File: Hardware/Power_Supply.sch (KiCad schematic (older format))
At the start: 14 parts, among them SW1 1101M2S3AQE2, U1 TPS565208DDC

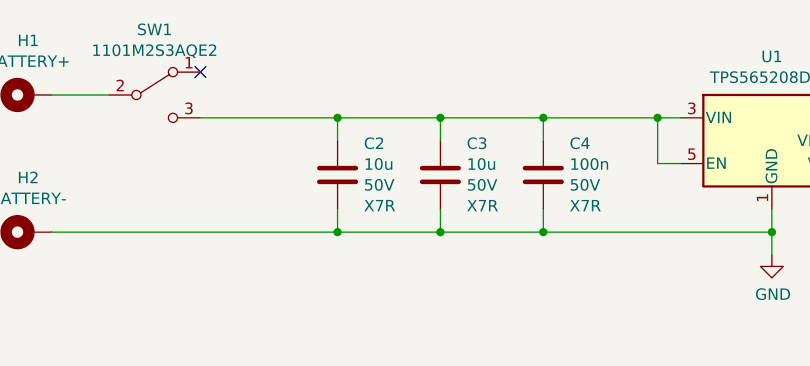
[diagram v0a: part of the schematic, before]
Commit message: [Hardware] Started ADC schematic sheet. Added ADC, voltage regulator and battery voltage sensing.
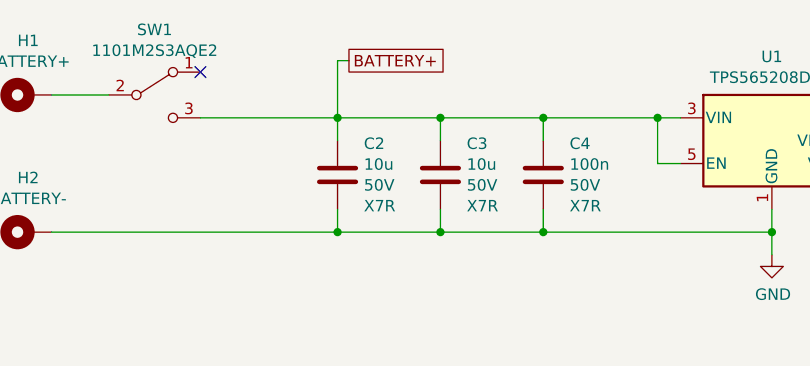
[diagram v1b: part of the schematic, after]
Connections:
- net BATTERY+: now reaches C2.2, C3.2, C4.2, SW1.3 (C), U1.3 (VIN), U1.5 (EN)
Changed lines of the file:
@@
 $Descr A4 11693 8268
 encoding utf-8
-Sheet 2 3
+Sheet 2 4
 Title "DC/DC power supply"
 Date "2020-07-27"
@@
 	2350 3350 2600 3350
 NoConn ~ 3000 3250
+Text GLabel 3650 3200 2    50   UnSpc ~ 0
+BATTERY+
+Wire Wire Line
+	3650 3200 3600 3200
+Wire Wire Line
+	3600 3200 3600 3450
 $EndSCHEMATC

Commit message: [Hardware] Added IHLP3232DZER3R3M01 inductor footprint.
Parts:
- L1: footprint (none) -> IHLP3232DZER3R3M01:IHLP3232DZER3R3M01
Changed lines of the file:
@@
 F 0 "L1" V 7290 3450 50  0000 C CNN
 F 1 "IHLP3232DZER3R3M01" V 7199 3450 50  0000 C CNN
-F 2 "" H 7100 3450 50  0001 C CNN
+F 2 "IHLP3232DZER3R3M01:IHLP3232DZER3R3M01" H 7100 3450 50  0001 C CNN
 F 3 "~" H 7100 3450 50  0001 C CNN
 F 4 "Vishay-Dale" H 7100 3450 50  0001 C CNN "Manufacturer"

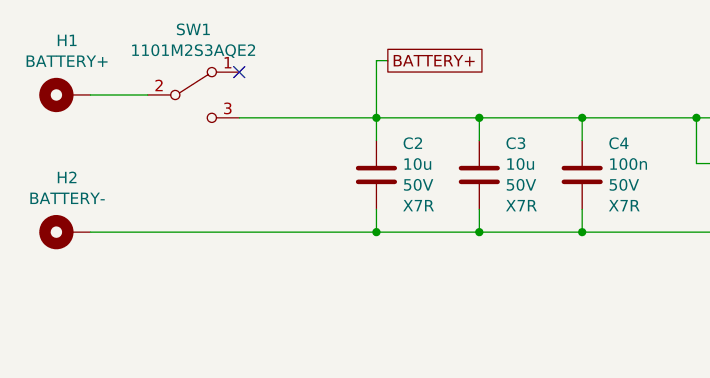
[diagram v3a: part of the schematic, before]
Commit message: [Hardware] Changed power switch pins order to ease routing.
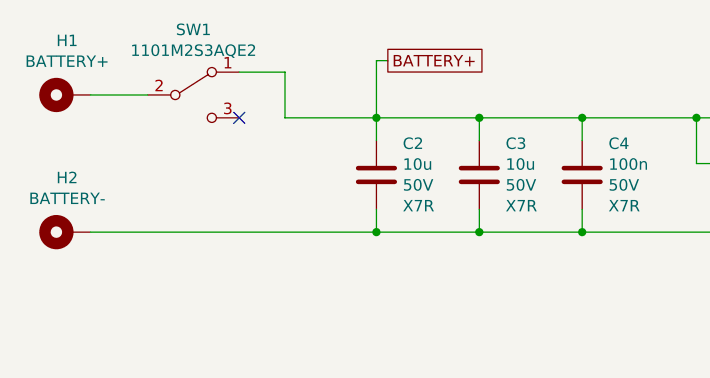
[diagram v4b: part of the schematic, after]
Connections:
- net BATTERY+: now also SW1.1 (A); no longer SW1.3 (C)
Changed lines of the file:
@@
 $EndComp
-Wire Wire Line
-	3000 3450 3600 3450
 Wire Wire Line
 	3600 3450 3600 3550
@@
 Wire Wire Line
 	2350 3350 2600 3350
-NoConn ~ 3000 3250
 Text GLabel 3650 3200 2    50   UnSpc ~ 0
 BATTERY+
@@
 Wire Wire Line
 	3600 3200 3600 3450
+Wire Wire Line
+	3000 3250 3200 3250
+Wire Wire Line
+	3200 3250 3200 3450
+Wire Wire Line
+	3200 3450 3600 3450
+NoConn ~ 3000 3450
 $EndSCHEMATC

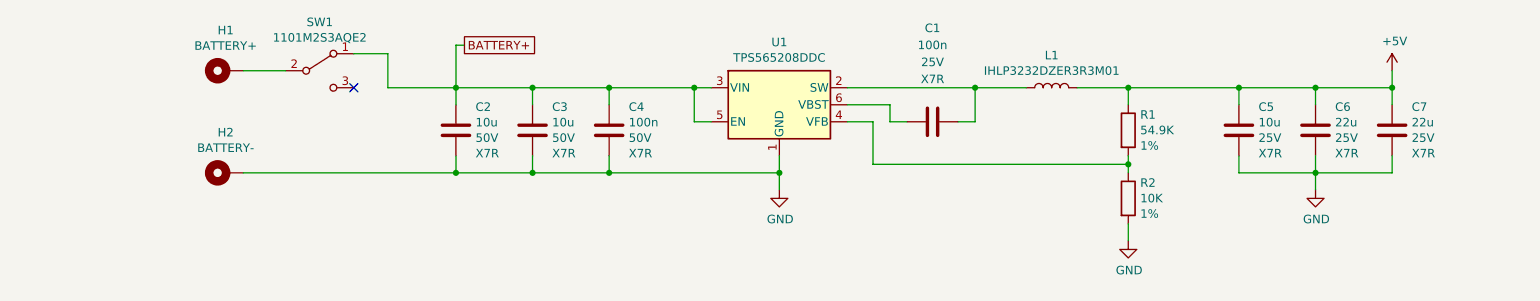
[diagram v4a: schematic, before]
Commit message: [Hardware] Removed mechanical supply parts unrelated with PCB, added battery holder supply part.
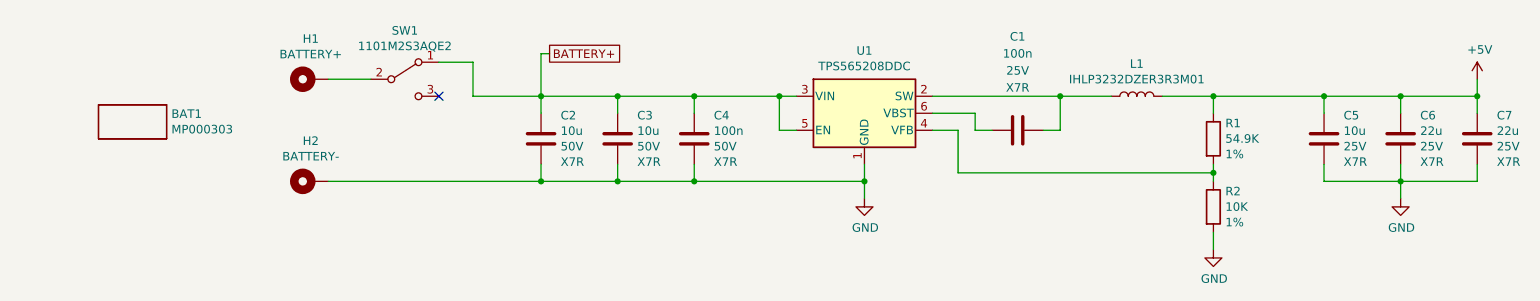
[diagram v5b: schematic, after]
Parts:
- added BAT1: MP000303, Supply_Part:Supply_Part, symbol Supply_Part:Supply_Part
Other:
- moved on the sheet: C1, C2, C3, C4, C5, C6, C7, H1, H2, L1, R1, R2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

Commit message: [Hardware] Changed 22u capacitors footprint from 1206 to 1210 as more references are available in 1210 package.
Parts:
- BAT1: Manufacturer Feetech -> MULTICOMP_PRO; Value2 Wheel -> Battery_Holder
- C6, C7: footprint Capacitor_SMD:C_1206_3216Metric_Pad1.42x1.75mm_HandSolder -> Capacitor_SMD:C_1210_3225Metric_Pad1.42x2.65mm_HandSolder
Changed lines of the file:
@@
 F 0 "C6" H 9035 3613 50  0000 R CNN
 F 1 "22u" H 9035 3704 50  0000 R CNN
-F 2 "Capacitor_SMD:C_1206_3216Metric_Pad1.42x1.75mm_HandSolder" H 9188 3600 50  0001 C CNN
+F 2 "Capacitor_SMD:C_1210_3225Metric_Pad1.42x2.65mm_HandSolder" H 9188 3600 50  0001 C CNN
 F 3 "~" H 9150 3750 50  0001 C CNN
 F 4 "25V" H 9035 3795 50  0000 R CNN "Value2"
@@
 F 0 "C7" H 9485 3613 50  0000 R CNN
 F 1 "22u" H 9485 3704 50  0000 R CNN
-F 2 "Capacitor_SMD:C_1206_3216Metric_Pad1.42x1.75mm_HandSolder" H 9638 3600 50  0001 C CNN
+F 2 "Capacitor_SMD:C_1210_3225Metric_Pad1.42x2.65mm_HandSolder" H 9638 3600 50  0001 C CNN
 F 3 "~" H 9600 3750 50  0001 C CNN
 F 4 "25V" H 9485 3795 50  0000 R CNN "Value2"
@@
 F 2 "Supply_Part:Supply_Part" H 1700 3650 50  0001 C CNN
 F 3 "" H 1700 3650 50  0001 C CNN
-F 4 "Feetech" H 1700 3650 50  0001 C CNN "Manufacturer"
-F 5 "Wheel" H 1700 3650 50  0001 C CNN "Value2"
+F 4 "MULTICOMP_PRO" H 1700 3650 50  0001 C CNN "Manufacturer"
+F 5 "Battery_Holder" H 1700 3650 50  0001 C CNN "Value2"
 	1    1700 3650
 	1    0    0    -1

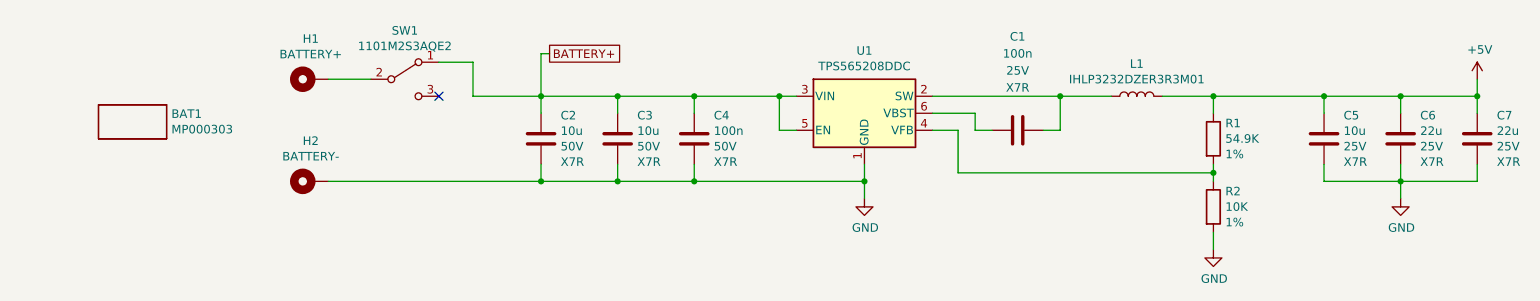
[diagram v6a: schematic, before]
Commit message: [Hardware] Added a big capacitor right after power supply switch to keep battery voltage stable during high current demands.
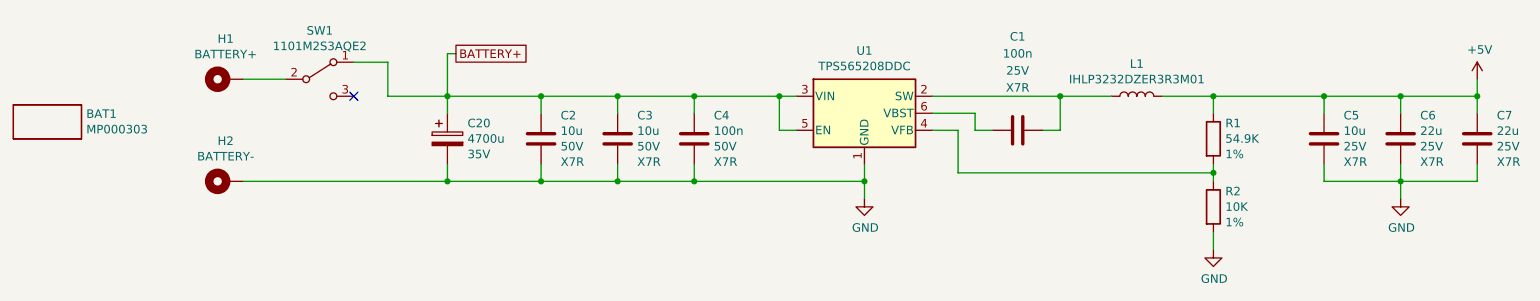
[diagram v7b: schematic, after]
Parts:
- added C20: 4700u, Capacitor_THT:CP_Radial_D16.0mm_P7.50mm, symbol Device:CP
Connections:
- net BATTERY+: now also C20.1
- net GND: now also C20.2
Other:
- moved on the sheet: BAT1, H1, H2, SW1
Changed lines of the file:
@@
 L Mechanical:MountingHole_Pad H2
 U 1 1 5F1FE00E
-P 2750 4000
-F 0 "H2" V 2987 4003 50  0000 C CNN
-F 1 "BATTERY-" V 2896 4003 50  0000 C CNN
-F 2 "MountingHole:MountingHole_2.2mm_M2_Pad" H 2750 4000 50  0001 C CNN
-F 3 "~" H 2750 4000 50  0001 C CNN
-	1    2750 4000
+P 2250 4000
+F 0 "H2" V 2487 4003 50  0000 C CNN
+F 1 "BATTERY-" V 2396 4003 50  0000 C CNN
+F 2 "MountingHole:MountingHole_2.2mm_M2_Pad" H 2250 4000 50  0001 C CNN
+F 3 "~" H 2250 4000 50  0001 C CNN
+	1    2250 4000
 	0    -1   -1   0
 $EndComp
@@
 L Mechanical:MountingHole_Pad H1
 U 1 1 5F1FF3A5
-P 2750 3400
-F 0 "H1" V 2987 3403 50  0000 C CNN
-F 1 "BATTERY+" V 2896 3403 50  0000 C CNN
-F 2 "MountingHole:MountingHole_2.2mm_M2_Pad" H 2750 3400 50  0001 C CNN
-F 3 "~" H 2750 3400 50  0001 C CNN
-	1    2750 3400
+P 2250 3400
+F 0 "H1" V 2487 3403 50  0000 C CNN
+F 1 "BATTERY+" V 2396 3403 50  0000 C CNN
+F 2 "MountingHole:MountingHole_2.2mm_M2_Pad" H 2250 3400 50  0001 C CNN
+F 3 "~" H 2250 3400 50  0001 C CNN
+	1    2250 3400
 	0    -1   -1   0
 $EndComp
@@
 Connection ~ 5000 4000
 Wire Wire Line
-	2850 4000 4100 4000
-Connection ~ 4100 4000
+	2350 4000 3550 4000
 Wire Wire Line
 	4100 4000 4550 4000
@@
 L Switch:SW_SPDT SW1
 U 1 1 5F22069E
-P 3300 3400
-F 0 "SW1" H 3300 3685 50  0000 C CNN
-F 1 "1101M2S3AQE2" H 3300 3594 50  0000 C CNN
-F 2 "1101M2S3AQE2:1101M2S3AQE2" H 3300 3400 50  0001 C CNN
-F 3 "~" H 3300 3400 50  0001 C CNN
-	1    3300 3400
-	1    0    0    -1
-$EndComp
-Wire Wire Line
-	2850 3400 3100 3400
-Text GLabel 4150 3250 2    50   UnSpc ~ 0
+P 2800 3400
+F 0 "SW1" H 2800 3685 50  0000 C CNN
+F 1 "1101M2S3AQE2" H 2800 3594 50  0000 C CNN
+F 2 "1101M2S3AQE2:1101M2S3AQE2" H 2800 3400 50  0001 C CNN
+F 3 "~" H 2800 3400 50  0001 C CNN
+	1    2800 3400
+	1    0    0    -1
+$EndComp
+Wire Wire Line
+	2350 3400 2600 3400
+Text GLabel 3600 3250 2    50   UnSpc ~ 0
 BATTERY+
 Wire Wire Line
-	4150 3250 4100 3250
-Wire Wire Line
-	4100 3250 4100 3500
-Wire Wire Line
-	3500 3300 3700 3300
-Wire Wire Line
-	3700 3300 3700 3500
-Wire Wire Line
-	3700 3500 4100 3500
-NoConn ~ 3500 3500
+	3600 3250 3550 3250
+Wire Wire Line
+	3550 3250 3550 3500
+Wire Wire Line
+	3000 3300 3200 3300
+Wire Wire Line
+	3200 3300 3200 3500
+NoConn ~ 3000 3500
 $Comp
 L Supply_Part:Supply_Part BAT?
 U 1 1 5F37F87A
-P 1700 3650
+P 1200 3650
 AR Path="/5F22814A/5F37F87A" Ref="BAT?"  Part="1"
 AR Path="/5F37F87A" Ref="BAT?"  Part="1"
 AR Path="/5F1F2F9E/5F37F87A" Ref="BAT1"  Part="1"
-F 0 "BAT1" H 1928 3696 50  0000 L CNN
-F 1 "MP000303" H 1928 3605 50  0000 L CNN
-F 2 "Supply_Part:Supply_Part" H 1700 3650 50  0001 C CNN
-F 3 "" H 1700 3650 50  0001 C CNN
-F 4 "MULTICOMP_PRO" H 1700 3650 50  0001 C CNN "Manufacturer"
-F 5 "Battery_Holder" H 1700 3650 50  0001 C CNN "Value2"
-	1    1700 3650
-	1    0    0    -1
-$EndComp
+F 0 "BAT1" H 1428 3696 50  0000 L CNN
+F 1 "MP000303" H 1428 3605 50  0000 L CNN
+F 2 "Supply_Part:Supply_Part" H 1200 3650 50  0001 C CNN
+F 3 "" H 1200 3650 50  0001 C CNN
+F 4 "MULTICOMP_PRO" H 1200 3650 50  0001 C CNN "Manufacturer"
+F 5 "Battery_Holder" H 1200 3650 50  0001 C CNN "Value2"
+	1    1200 3650
+	1    0    0    -1
+$EndComp
+$Comp
+L Device:CP C20
+U 1 1 5F467D3F
+P 3550 3750
+F 0 "C20" H 3668 3841 50  0000 L CNN
+F 1 "4700u" H 3668 3750 50  0000 L CNN
+F 2 "Capacitor_THT:CP_Radial_D16.0mm_P7.50mm" H 3588 3600 50  0001 C CNN
+F 3 "~" H 3550 3750 50  0001 C CNN
+F 4 "35V" H 3668 3659 50  0000 L CNN "Value2"
+F 5 "MCKSK035M472J32S" H 3550 3750 50  0001 C CNN "Value3"
+	1    3550 3750
+	1    0    0    -1
+$EndComp
+Wire Wire Line
+	3200 3500 3550 3500
+Wire Wire Line
+	3550 3500 4100 3500
+Connection ~ 3550 3500
+Wire Wire Line
+	3550 3500 3550 3600
+Wire Wire Line
+	3550 3900 3550 4000
+Connection ~ 3550 4000
+Connection ~ 4100 4000
+Wire Wire Line
+	3550 4000 4100 4000
 $EndSCHEMATC

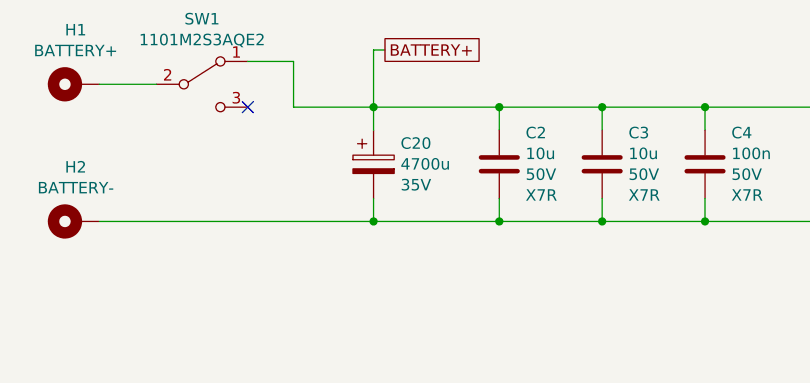
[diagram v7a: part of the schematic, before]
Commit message: [Hardware] Added big capacitor 'custom' footprint to PCB. Capacitor must be bent over SMD parts and glued like shown in pictures.
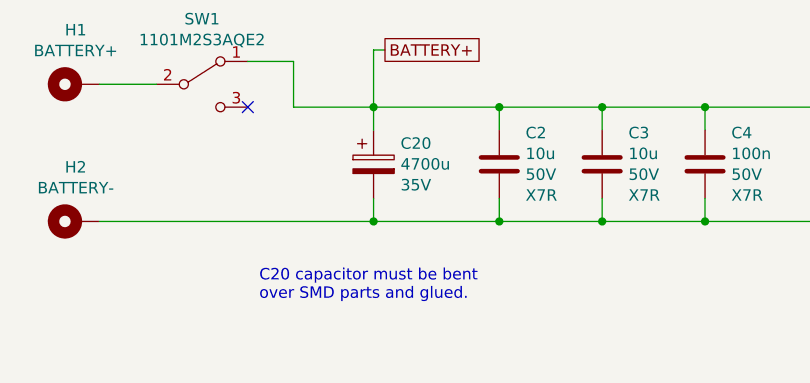
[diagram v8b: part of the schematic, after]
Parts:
- C20: footprint Capacitor_THT:CP_Radial_D16.0mm_P7.50mm -> Capacitor_THT:C_Rect_L9.0mm_W2.5mm_P7.50mm_MKT
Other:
- note added: "C20 capacitor must be bent\nover SMD parts and glued."
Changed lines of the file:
@@
 F 0 "C20" H 3668 3841 50  0000 L CNN
 F 1 "4700u" H 3668 3750 50  0000 L CNN
-F 2 "Capacitor_THT:CP_Radial_D16.0mm_P7.50mm" H 3588 3600 50  0001 C CNN
+F 2 "Capacitor_THT:C_Rect_L9.0mm_W2.5mm_P7.50mm_MKT" H 3588 3600 50  0001 C CNN
 F 3 "~" H 3550 3750 50  0001 C CNN
 F 4 "35V" H 3668 3659 50  0000 L CNN "Value2"
@@
 Wire Wire Line
 	3550 4000 4100 4000
+Text Notes 3050 4350 0    50   ~ 0
+C20 capacitor must be bent\nover SMD parts and glued.
 $EndSCHEMATC
